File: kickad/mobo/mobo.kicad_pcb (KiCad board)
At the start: 2 copper layers, 124.1 x 130 mm, 30 parts, among them J1 nice!view, J10 rgb, J11 rows, J12 columns, J13 columns, J2 Battery, J4 rotary, J5 trackball, J6 nice!view, J7 Battery, J8 rgb, J9 rows, SW1 Power, SW2 Reset, SW3 Reset, SW4 Power, U1 nice!nano v2, U3 nice!nano v2

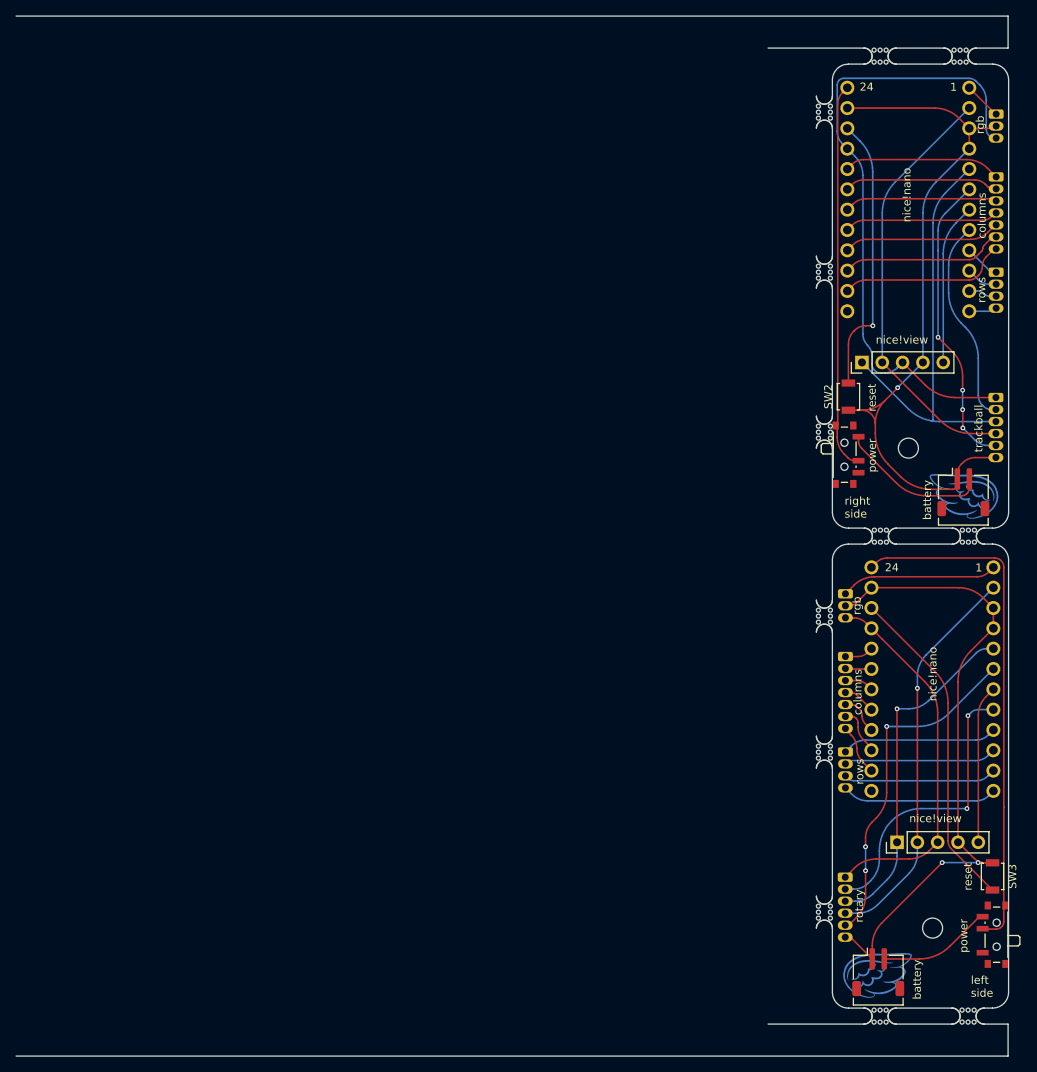
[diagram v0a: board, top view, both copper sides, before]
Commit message: Resetting the mobo stack to 4 layers mirrorable
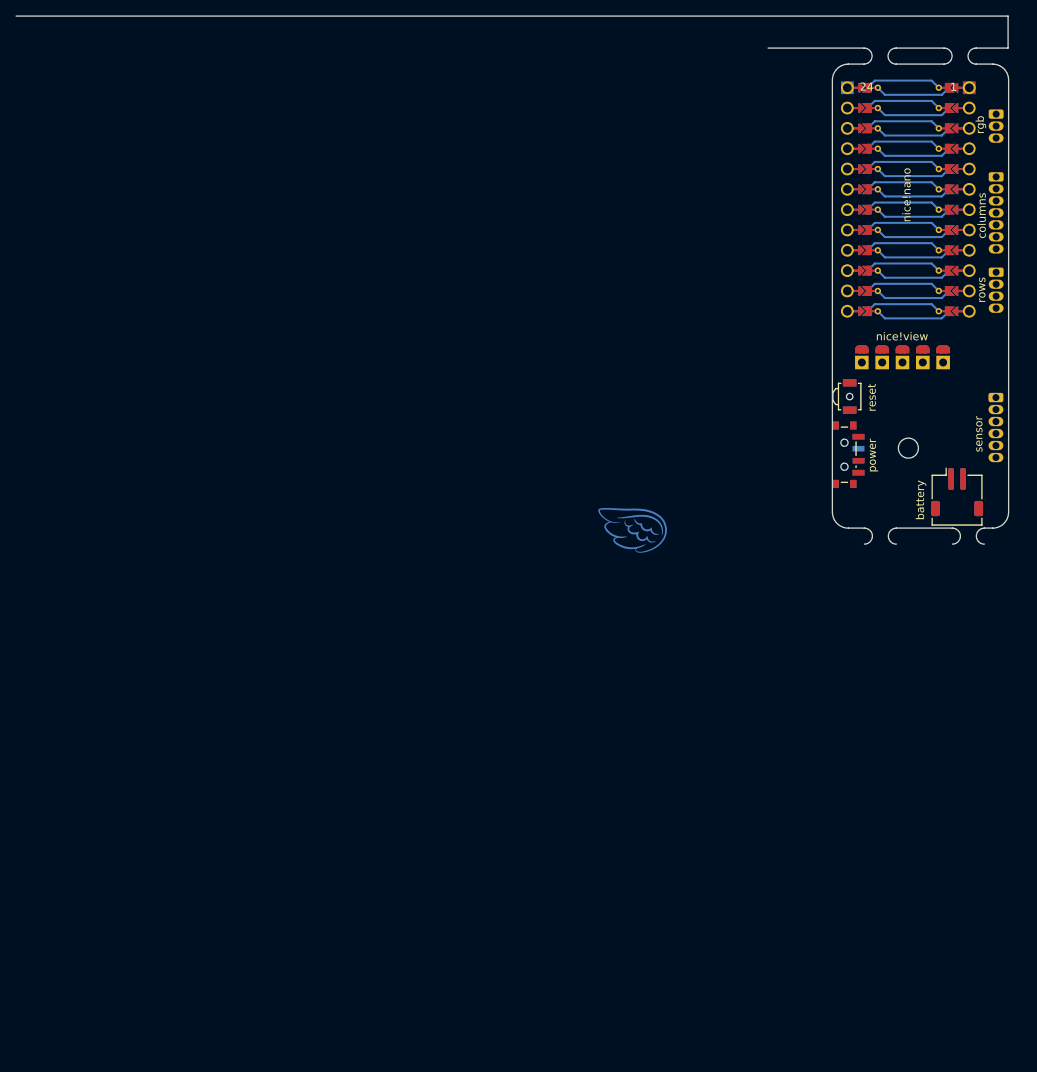
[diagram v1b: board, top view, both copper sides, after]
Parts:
- removed J10: rgb, Connector_Wuerth:Wuerth_WR-WTB_64800311622_1x03_P1.50mm_Vertical
- removed J11: rows, Connector_Wuerth:Wuerth_WR-WTB_64800411622_1x04_P1.50mm_Vertical
- removed J13: columns, Connector_Wuerth:Wuerth_WR-WTB_64800711622_1x07_P1.50mm_Vertical
- removed J5: trackball, Connector_Wuerth:Wuerth_WR-WTB_64800611622_1x06_P1.50mm_Vertical
- removed J6: nice!view, Connector_PinHeader_2.54mm:PinHeader_1x05_P2.54mm_Vertical
- removed J7: Battery, Connector_JST:JST_ZH_S2B-ZR-SM4A-TF_1x02-1MP_P1.50mm_Horizontal
- removed SW3: Reset, Button_Switch_SMD:SW_SPST_B3U-1000P
- removed SW4: Power, Button_Switch_SMD:SW_SPDT_PCM12
- removed U3: nice!nano v2, ScottoKeebs_MCU:Nice_Nano_V2_Flipped
- removed mouse-bite-2mm-slot (x12): VAL**, Panelization:mouse-bite-2mm-slot
- J1: footprint Connector_PinHeader_2.54mm:PinHeader_1x05_P2.54mm_Vertical -> display:OLED-128x32-double-sided
- J4: value rotary -> sensor
- SW2: footprint Button_Switch_SMD:SW_SPST_B3U-1000P -> Button_Switch_SMD:SW_SPST_B3U-3000P-B
- U1: footprint ScottoKeebs_MCU:Nice_Nano_V2_Flipped -> keyboard_reversible:ProMicro_flipped
- moved J1 3.30 mm to (188.6, 70.9)
- moved J2 0.79 mm to (197.6, 85.5)
- moved SW2 0.15 mm to (184.2, 73.6)
- turned U1 to -90 degrees
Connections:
- net BAT L renamed BAT
- net CS_D L renamed CS_D
- net CS_T L renamed CS_T
- net Col 0 L renamed Col 0
- net Col 1 L renamed Col 1
- net Col 2 L renamed Col 2
- net Col 3 L renamed Col 3
- net Col 4 L renamed Col 4
- net Col 5 L renamed Col 5
- net Col 6 L renamed Col 6
- net GND L renamed GND
- net IRQ L renamed IRQ
- net RGB L renamed RGB
- net RST L renamed RST
- net Row 0 L renamed Row 0
- net Row 1 L renamed Row 1
- net Row 2 L renamed Row 2
- net Row 3 L renamed Row 3
- net SCK L renamed SCK
- net SDIO L renamed SDIO
- net VCC L renamed VCC
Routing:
- net GND: track 91.0 -> 0.00 mm, vias 1 -> 0
- net GND R: track 80.8 -> 0.00 mm, vias 2 -> 0
- net VCC: track 80.5 -> 0.00 mm
- net BAT R: track 65.1 -> 0.00 mm
- net SCK: track 53.7 -> 0.00 mm
- net SDIO: track 52.9 -> 0.00 mm
- net SCK R: track 49.6 -> 0.00 mm, vias 1 -> 0
- net BAT: track 48.5 -> 0.00 mm
- net VCC R: track 46.6 -> 0.00 mm
- net SDIO R: track 42.8 -> 0.00 mm, vias 1 -> 0
- net IRQ R: track 42.7 -> 0.00 mm, vias 3 -> 0
- net RST R: track 41.2 -> 0.00 mm
- net IRQ: track 37.3 -> 0.00 mm, vias 4 -> 0
- net CS_T R: track 36.5 -> 0.00 mm, vias 2 -> 0
- net RST: track 34.9 -> 0.00 mm, vias 1 -> 0
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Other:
- board size 124.1 x 130 mm -> 124.1 x 66 mm
- copper layers 2 -> 4
- board text added: "sensor"
- board text removed: "left side"
- board text removed: "right side"
- board text removed: "rotary"
- board text removed: "trackball"

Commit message: Reworking the mobo into a reversible panel
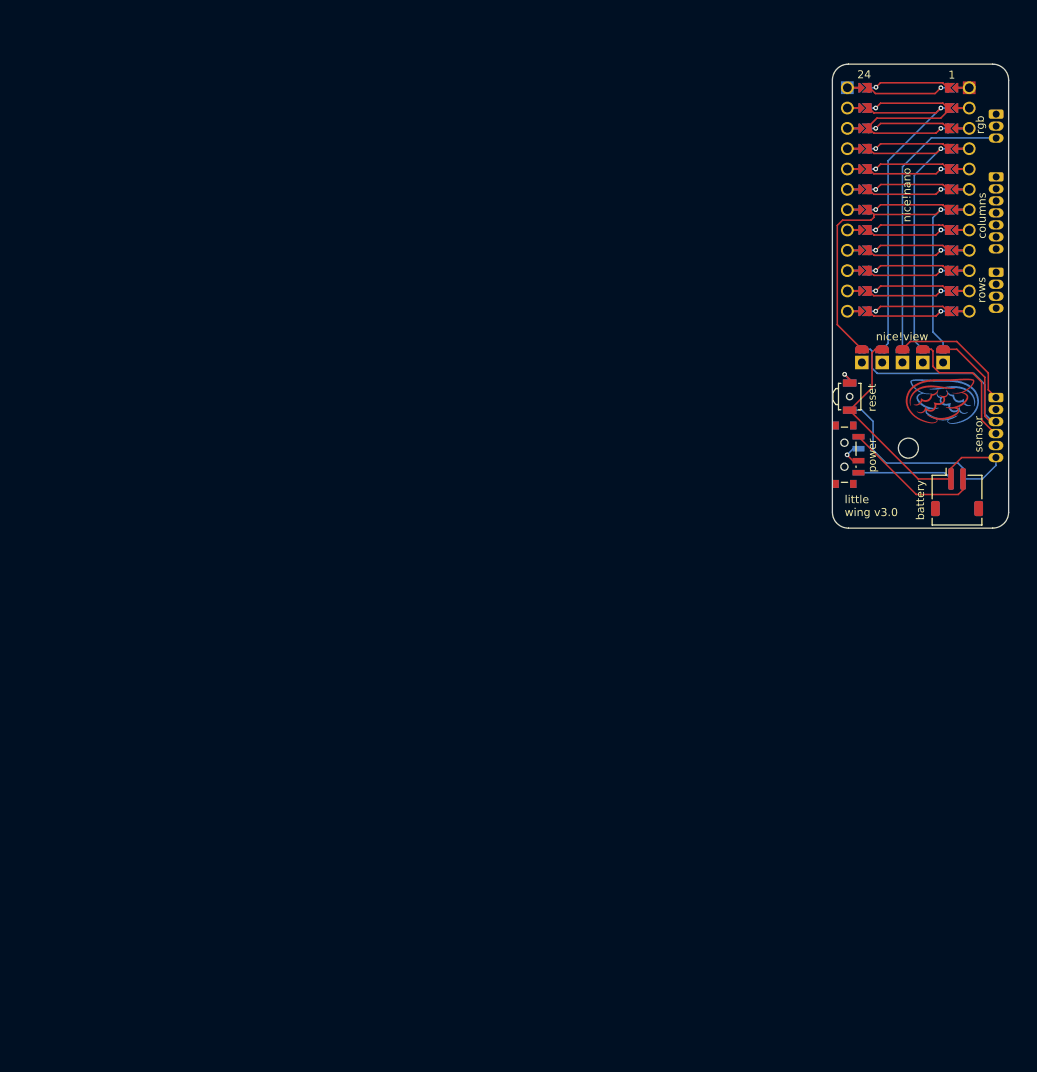
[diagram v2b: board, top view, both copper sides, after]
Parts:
- U1: footprint keyboard_reversible:ProMicro_flipped -> keyboard_reversible:ProMicro_independent_flipped
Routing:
- net GND: track 0.00 -> 189.9 mm, vias 0 -> 3
- net VCC: track 0.00 -> 119.6 mm, vias 0 -> 1
- net SCK: track 0.00 -> 118.5 mm, vias 0 -> 1
- net SDIO: track 0.00 -> 96.2 mm, vias 0 -> 1
- net BAT: track 0.00 -> 66.2 mm, vias 0 -> 2
- net CS_D: track 0.00 -> 50.7 mm, vias 0 -> 1
- net RST: track 0.00 -> 50.1 mm, vias 0 -> 2
- net IRQ: track 0.00 -> 46.3 mm, vias 0 -> 1
- net CS_T: track 0.00 -> 36.5 mm, vias 0 -> 1
- net Net-(J2-Pin_2): track 0.00 -> 29.5 mm
- net Col 6: track 0.00 -> 28.1 mm, vias 0 -> 1
- net Col 5: track 0.00 -> 27.5 mm, vias 0 -> 1
- net Col 0: track 0.00 -> 26.7 mm, vias 0 -> 1
- net Col 4: track 0.00 -> 26.6 mm, vias 0 -> 1
- net Col 1: track 0.00 -> 26.3 mm, vias 0 -> 1
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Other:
- board size 124.1 x 66 mm -> 22 x 58 mm
- board text added: "little wing v3.0"
- board text removed: "little wing v2.1"

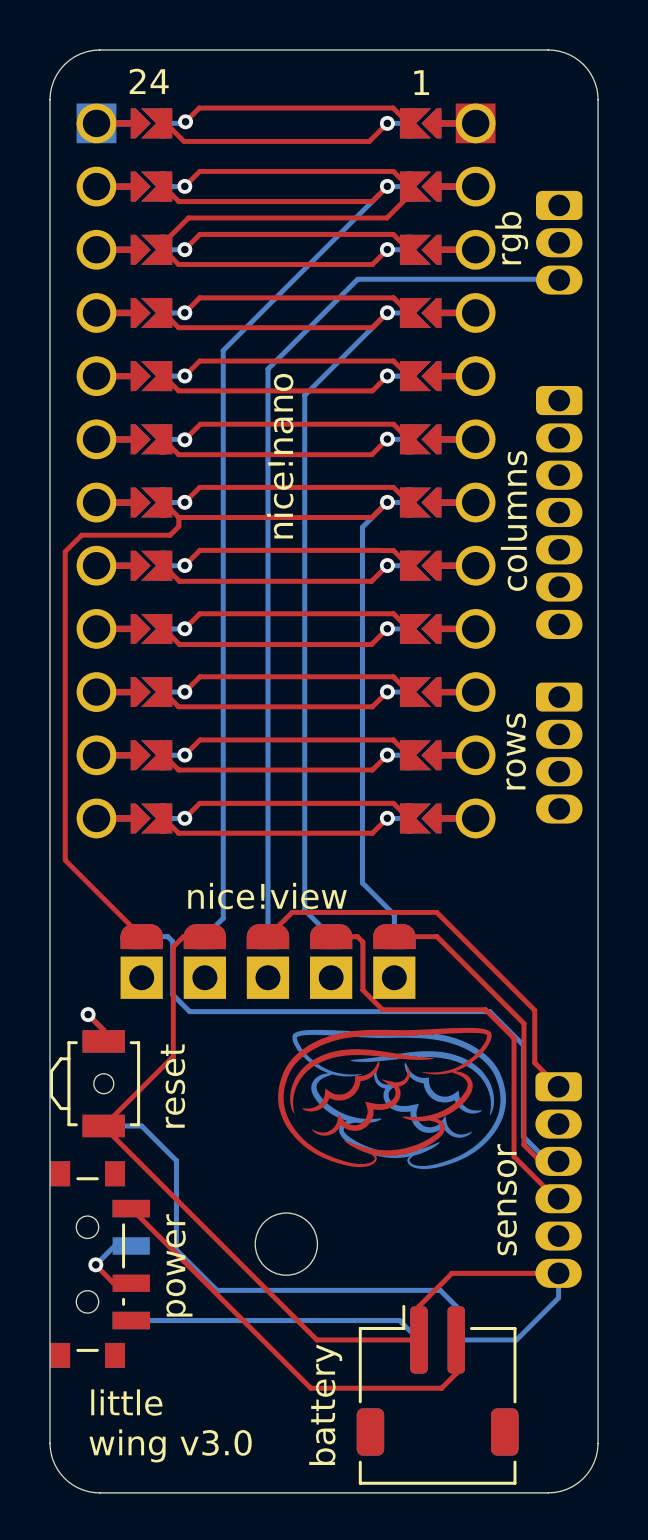
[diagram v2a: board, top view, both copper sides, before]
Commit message: Reworking the keypad PCB
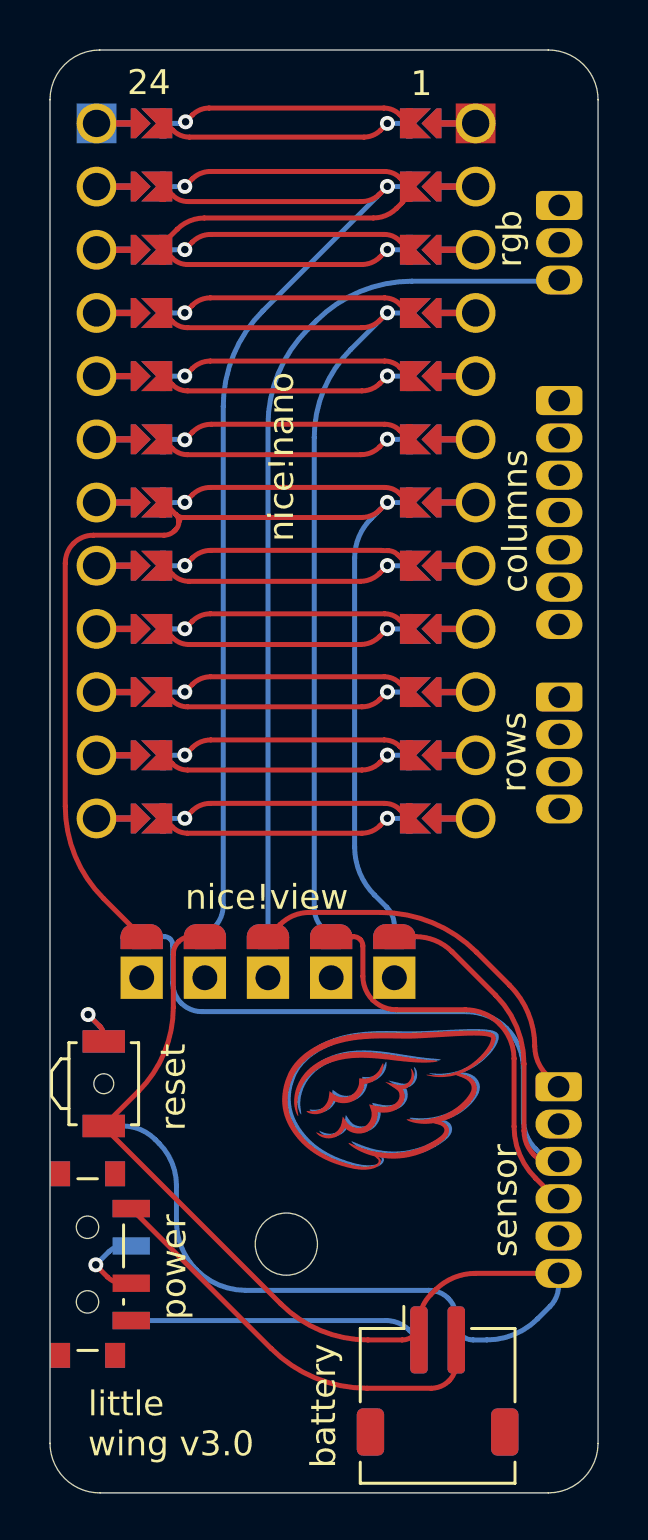
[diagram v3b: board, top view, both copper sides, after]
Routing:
- net GND: track 189.9 -> 185.4 mm
- net VCC: track 119.6 -> 117.2 mm
- net SDIO: track 96.2 -> 94.3 mm
- net SCK: track 118.5 -> 116.6 mm
- net IRQ: track 46.3 -> 45.6 mm
- net CS_T: track 36.5 -> 35.9 mm
- net RGB: track 18.5 -> 18.0 mm
